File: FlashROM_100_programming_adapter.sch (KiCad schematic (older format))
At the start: 5 parts, among them J1 LH535618 DIP LEGS, U1 28C256

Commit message: Add FlashROM_100. /WE pin on FlexROM_100
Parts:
- removed JP1: ~CS~ breakout (REX TP1), 000_LOCAL:Pin_Header_Angled_1x02_Pitch2.54mm, symbol 000_LOCAL:Jumper_2_Bridged
- removed R1, R2: 47K, 000_LOCAL:R_0805, symbol 000_LOCAL:R_US
- J1: value LH535618 DIP LEGS -> LH535618 Socket; footprint 000_LOCAL:DIP28_0.6_pcb_sil_pins -> 000_LOCAL:DIP28_0.6
- U1: value 28C256 -> 29F010 pinout to programmer; footprint 000_LOCAL:SOIC28W -> 000_LOCAL:DIP32_0.3; symbol 000_LOCAL:28C256 -> 000_LOCAL:SST39SF010_PLCC
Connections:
- net ~CS_IN is gone; now on net D6: U1.20 (DQ6)
- net A0: now also U1.12 (A0); no longer U1.10 (A0)
- net A1: now also U1.11 (A1); no longer U1.9 (A1)
- net A10: now also U1.23 (A10); no longer U1.21 (A10)
- net A11: now also U1.25 (A11); no longer U1.23 (A11)
- net A12: now also U1.4 (A12); no longer U1.2 (A12)
- net A13: now also U1.28 (A13); no longer U1.26 (A13)
- net A14: now also U1.29 (A14); no longer U1.1 (A14)
- net A2: now also U1.10 (A2); no longer U1.8 (A2)
- net A3: now also U1.9 (A3); no longer U1.7 (A3)
- net A4: now also U1.8 (A4); no longer U1.6 (A4)
- net A5: now also U1.7 (A5); no longer U1.5 (A5)
- net A6: now also U1.6 (A6); no longer U1.4 (A6)
- net A7: now also U1.5 (A7); no longer U1.3 (A7)
- net A8: now also U1.27 (A8); no longer U1.25 (A8)
- net A9: now also U1.26 (A9); no longer U1.24 (A9)
- net D0: now also U1.13 (DQ0); no longer U1.11 (D0)
- net D1: now also U1.14 (DQ1); no longer U1.12 (D1)
- net D2: now also U1.15 (DQ2); no longer U1.13 (D2)
- net D3: now also U1.17 (DQ3); no longer U1.15 (D3)
- net D4: now also U1.18 (DQ4); no longer U1.16 (D4)
- net D5: now also U1.19 (DQ5); no longer U1.17 (D5)
- net D6: no longer U1.18 (D6)
- net D7: now also U1.21 (DQ7); no longer U1.19 (D7)
- net GND: now also U1.16 (VSS); no longer U1.14 (GND)
- net VCC: now also U1.32 (VDD); no longer U1.28 (VCC)
- net ~OE: now also U1.24 (~OE); no longer U1.22 (~OE)
- net ~WE: now also U1.31 (~WE); no longer U1.27 (~WE)
- net ~CS_OUT renamed ~CE
- net ~CE: now also U1.22 (~CE)
- no-connect marks 0 -> 4
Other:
- note added: "FlashROM_100 programming adapter.\n\nPlace this board into programmer.\nPlace FlashROM_100 into the DIP-28 socket.\n\nThis for the 29F010 FlashROM_100, not the 28C256 FlexROM_100."
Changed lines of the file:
@@
 encoding utf-8
 Sheet 1 1
-Title "28C256 SOIC to LH535618 DIP"
-Date ""
+Title "29F010 to LH535618 programming adapter"
+Date "2020-11-05"
 Rev ""
-Comp ""
-Comment1 "TRS-80 Model 100 system rom M12"
-Comment2 "With REX main ROM support"
+Comp "b.kenyon.w@gmail.com"
+Comment1 ""
+Comment2 ""
 Comment3 ""
 Comment4 ""
 $EndDescr
 $Comp
-L 000_LOCAL:28C256 U1
+L 000_LOCAL:SST39SF010_PLCC U1
 U 1 1 5E5B130A
-P 6670 3040
-F 0 "U1" H 6810 4160 50  0000 C CNN
-F 1 "28C256" H 6670 4350 50  0000 C CNN
-F 2 "000_LOCAL:SOIC28W" H 6670 3040 50  0001 C CNN
-F 3 "http://ww1.microchip.com/downloads/en/DeviceDoc/doc0006.pdf" H 6670 3040 50  0001 C CNN
-	1    6670 3040
+P 6700 3340
+F 0 "U1" H 6840 4460 50  0000 C CNN
+F 1 "29F010 pinout to programmer" H 6700 5060 50  0000 C CNN
+F 2 "000_LOCAL:DIP32_0.3" H 6700 3340 50  0001 C CNN
+F 3 "http://ww1.microchip.com/downloads/en/DeviceDoc/doc0006.pdf" H 6700 3340 50  0001 C CNN
+	1    6700 3340
 	1    0    0    -1
 $EndComp
@@
 P 4260 3040
 F 0 "J1" H 4440 4190 50  0000 C CNN
-F 1 "LH535618 DIP LEGS" H 4260 4420 50  0000 C CNN
-F 2 "000_LOCAL:DIP28_0.6_pcb_sil_pins" H 4260 3040 50  0001 C CNN
+F 1 "LH535618 Socket" H 4260 4420 50  0000 C CNN
+F 2 "000_LOCAL:DIP28_0.6" H 4260 3040 50  0001 C CNN
 F 3 "http://ww1.microchip.com/downloads/en/DeviceDoc/doc0014.pdf" H 4260 3040 50  0001 C CNN
 	1    4260 3040
@@
 	3400 3840 3500 3940
 Entry Wire Line
-	5830 1840 5930 1940
-Entry Wire Line
-	5830 3640 5930 3740
-Entry Wire Line
-	5830 4040 5930 4140
+	5830 1890 5930 1990
+Entry Wire Line
+	5830 4140 5930 4240
 Entry Wire Line
 	5830 2140 5930 2240
@@
 Entry Wire Line
 	5830 3440 5930 3540
-Text Label 5930 1940 0    50   ~ 0
+Text Label 5930 1990 0    50   ~ 0
 VCC
-Text Label 5930 3740 0    50   ~ 0
+Text Label 5930 4240 0    50   ~ 0
 ~WE
-Text Label 5930 4140 0    50   ~ 0
-GND
-Entry Wire Line
-	5830 3740 5930 3840
-Entry Wire Line
-	5830 3840 5930 3940
+Entry Wire Line
+	5830 4340 5930 4440
+Entry Wire Line
+	5830 4240 5930 4340
 Entry Wire Line
 	3400 1840 3500 1940
@@
 ~OE
 Text Label 3500 3940 0    50   ~ 0
-~CS_OUT
-Text Label 5930 3840 0    50   ~ 0
+~CE
+Text Label 5930 4440 0    50   ~ 0
 ~OE
-Text Label 5930 3940 0    50   ~ 0
-~CS_IN
+Text Label 5930 4340 0    50   ~ 0
+~CE
 Text Label 3500 2240 0    50   ~ 0
 A1
@@
 D7
 Entry Wire Line
-	7300 2140 7400 2040
-Entry Wire Line
-	7300 2240 7400 2140
-Entry Wire Line
-	7300 2340 7400 2240
-Entry Wire Line
-	7300 2440 7400 2340
-Entry Wire Line
-	7300 2540 7400 2440
-Entry Wire Line
-	7300 2640 7400 2540
-Entry Wire Line
-	7300 2740 7400 2640
-Entry Wire Line
-	7300 2840 7400 2740
-Text Label 7300 2140 2    50   ~ 0
+	7530 2140 7630 2040
+Entry Wire Line
+	7530 2240 7630 2140
+Entry Wire Line
+	7530 2340 7630 2240
+Entry Wire Line
+	7530 2440 7630 2340
+Entry Wire Line
+	7530 2540 7630 2440
+Entry Wire Line
+	7530 2640 7630 2540
+Entry Wire Line
+	7530 2740 7630 2640
+Entry Wire Line
+	7530 2840 7630 2740
+Text Label 7530 2140 2    50   ~ 0
 D0
-Text Label 7300 2240 2    50   ~ 0
+Text Label 7530 2240 2    50   ~ 0
 D1
-Text Label 7300 2340 2    50   ~ 0
+Text Label 7530 2340 2    50   ~ 0
 D2
-Text Label 7300 2440 2    50   ~ 0
+Text Label 7530 2440 2    50   ~ 0
 D3
-Text Label 7300 2540 2    50   ~ 0
+Text Label 7530 2540 2    50   ~ 0
 D4
-Text Label 7300 2640 2    50   ~ 0
+Text Label 7530 2640 2    50   ~ 0
 D5
-Text Label 7300 2740 2    50   ~ 0
+Text Label 7530 2740 2    50   ~ 0
 D6
-Text Label 7300 2840 2    50   ~ 0
+Text Label 7530 2840 2    50   ~ 0
 D7
-Entry Wire Line
-	3400 4570 3500 4670
-Entry Wire Line
-	3400 4670 3500 4770
-$Comp
-L 000_LOCAL:Jumper_2_Bridged JP1
-U 1 1 5E68B8A2
-P 4020 4670
-F 0 "JP1" H 4020 4750 50  0000 C CNN
-F 1 "~CS~ breakout (REX TP1)" H 4020 4830 50  0000 C CNN
-F 2 "000_LOCAL:Pin_Header_Angled_1x02_Pitch2.54mm" H 4020 4670 50  0001 C CNN
-F 3 "~" H 4020 4670 50  0001 C CNN
-	1    4020 4670
-	-1   0    0    -1
-$EndComp
-Entry Wire Line
-	3400 4770 3500 4870
-$Comp
-L 000_LOCAL:R_US R2
-U 1 1 5E68C7F8
-P 4080 4870
-F 0 "R2" V 4040 4550 50  0000 C CNN
-F 1 "47K" V 4040 4700 50  0000 C CNN
-F 2 "000_LOCAL:R_0805" H 4080 4870 50  0001 C CNN
-F 3 "~" H 4080 4870 50  0001 C CNN
-	1    4080 4870
-	0    1    1    0
-$EndComp
-Wire Wire Line
-	3500 4670 3820 4670
-Text Label 3500 4670 0    50   ~ 0
-~CS_OUT
-Wire Wire Line
-	3500 4870 3930 4870
-Text Label 3500 4770 0    50   ~ 0
-~CS_IN
-Text Label 3500 4870 0    50   ~ 0
-VCC
 Wire Bus Line
 	3400 5540 4980 5540
-Connection ~ 5830 5540
-Wire Bus Line
-	5830 5540 7400 5540
-Entry Wire Line
-	3400 5070 3500 5170
-Entry Wire Line
-	3400 5170 3500 5270
-$Comp
-L 000_LOCAL:R_US R1
-U 1 1 5E6B3AF8
-P 4080 5270
-F 0 "R1" V 4030 4900 50  0000 C CNN
-F 1 "47K" V 4030 5040 50  0000 C CNN
-F 2 "000_LOCAL:R_0805" H 4080 5270 50  0001 C CNN
-F 3 "~" H 4080 5270 50  0001 C CNN
-	1    4080 5270
-	0    1    1    0
-$EndComp
-Wire Wire Line
-	3500 5270 3930 5270
-Wire Wire Line
-	4230 5270 4230 5170
-Text Label 3500 5270 0    50   ~ 0
-VCC
-Text Label 3500 5170 0    50   ~ 0
-~WE
 Connection ~ 4980 5540
-Wire Bus Line
-	4980 5540 5830 5540
-Wire Bus Line
-	5830 5540 6590 5540
 Wire Wire Line
 	3500 1940 4260 1940
@@
 	4660 2840 4880 2840
 Wire Wire Line
-	5930 1940 6670 1940
-Wire Wire Line
-	5930 2140 6270 2140
-Wire Wire Line
-	5930 2240 6270 2240
-Wire Wire Line
-	5930 2340 6270 2340
-Wire Wire Line
-	5930 2440 6270 2440
-Wire Wire Line
-	5930 2540 6270 2540
-Wire Wire Line
-	5930 2640 6270 2640
-Wire Wire Line
-	5930 2740 6270 2740
-Wire Wire Line
-	5930 2840 6270 2840
-Wire Wire Line
-	5930 2940 6270 2940
-Wire Wire Line
-	5930 3040 6270 3040
-Wire Wire Line
-	5930 3140 6270 3140
-Wire Wire Line
-	5930 3240 6270 3240
-Wire Wire Line
-	5930 3340 6270 3340
-Wire Wire Line
-	5930 3440 6270 3440
-Wire Wire Line
-	5930 3540 6270 3540
-Wire Wire Line
-	5930 3740 6270 3740
-Wire Wire Line
-	5930 3840 6270 3840
-Wire Wire Line
-	5930 3940 6270 3940
-Wire Wire Line
-	5930 4140 6670 4140
-Wire Wire Line
-	7070 2140 7300 2140
-Wire Wire Line
-	7070 2240 7300 2240
-Wire Wire Line
-	7070 2340 7300 2340
-Wire Wire Line
-	7070 2440 7300 2440
-Wire Wire Line
-	7070 2540 7300 2540
-Wire Wire Line
-	7070 2640 7300 2640
-Wire Wire Line
-	7070 2740 7300 2740
-Wire Wire Line
-	7070 2840 7300 2840
-Wire Wire Line
-	4360 4670 4360 4770
-Wire Wire Line
-	4230 4870 4360 4870
-Wire Wire Line
-	3500 4770 4360 4770
-Connection ~ 4360 4770
-Wire Wire Line
-	4360 4770 4360 4870
-Wire Wire Line
-	4360 4670 4220 4670
-Wire Wire Line
-	3500 5170 4230 5170
+	7300 2140 7530 2140
+Wire Wire Line
+	7300 2240 7530 2240
+Wire Wire Line
+	7300 2340 7530 2340
+Wire Wire Line
+	7300 2440 7530 2440
+Wire Wire Line
+	7300 2540 7530 2540
+Wire Wire Line
+	7300 2640 7530 2640
+Wire Wire Line
+	7300 2740 7530 2740
+Wire Wire Line
+	7300 2840 7530 2840
 Entry Wire Line
 	3400 3640 3500 3740
 Wire Wire Line
-	3500 3740 3860 3740
-Wire Bus Line
-	4980 2040 4980 5540
-Wire Bus Line
-	7400 2040 7400 5540
-Wire Bus Line
-	5830 1840 5830 5540
-Wire Bus Line
-	3400 1840 3400 5540
+	3860 3740 3500 3740
 Text Label 3500 3740 0    50   ~ 0
 ~WE
+NoConn ~ 6100 3740
+NoConn ~ 6100 3640
+Entry Wire Line
+	5830 4490 5930 4590
+Text Label 5930 4590 0    50   ~ 0
+GND
+Wire Wire Line
+	5930 1990 6700 1990
+Wire Wire Line
+	5930 2140 6100 2140
+Wire Wire Line
+	5930 2240 6100 2240
+Wire Wire Line
+	5930 2340 6100 2340
+Wire Wire Line
+	5930 2440 6100 2440
+Wire Wire Line
+	5930 2540 6100 2540
+Wire Wire Line
+	5930 2640 6100 2640
+Wire Wire Line
+	5930 2740 6100 2740
+Wire Wire Line
+	5930 2840 6100 2840
+Wire Wire Line
+	5930 2940 6100 2940
+Wire Wire Line
+	5930 3040 6100 3040
+Wire Wire Line
+	5930 3140 6100 3140
+Wire Wire Line
+	5930 3240 6100 3240
+Wire Wire Line
+	5930 3340 6100 3340
+Wire Wire Line
+	5930 3440 6100 3440
+Wire Wire Line
+	5930 3540 6100 3540
+Wire Wire Line
+	5930 4240 6100 4240
+Wire Wire Line
+	5930 4340 6100 4340
+Wire Wire Line
+	5930 4440 6100 4440
+Wire Wire Line
+	5930 4590 6700 4590
+NoConn ~ 7300 4340
+NoConn ~ 7300 4440
+Wire Bus Line
+	4980 5540 7630 5540
+Wire Bus Line
+	4980 2040 4980 5540
+Wire Bus Line
+	7630 2040 7630 5540
+Wire Bus Line
+	3400 1840 3400 5540
+Wire Bus Line
+	5830 1890 5830 5540
+Text Notes 4440 6170 0    50   ~ 0
+FlashROM_100 programming adapter.\n\nPlace this board into programmer.\nPlace FlashROM_100 into the DIP-28 socket.\n\nThis for the 29F010 FlashROM_100, not the 28C256 FlexROM_100.
 $EndSCHEMATC

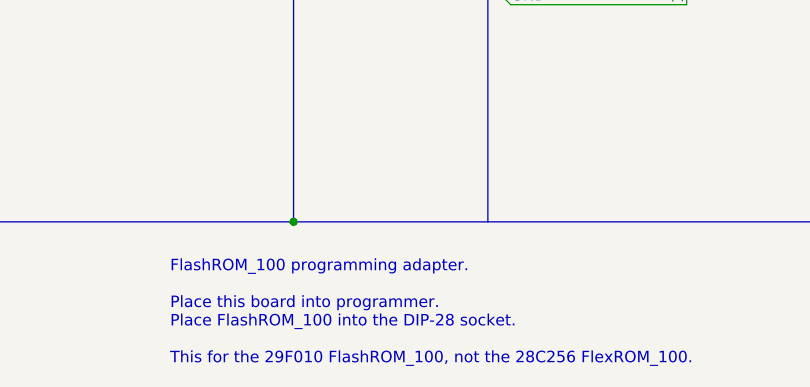
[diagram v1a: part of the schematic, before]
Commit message: FlexROM_100 & FlashROM_100 fix ALE/WE
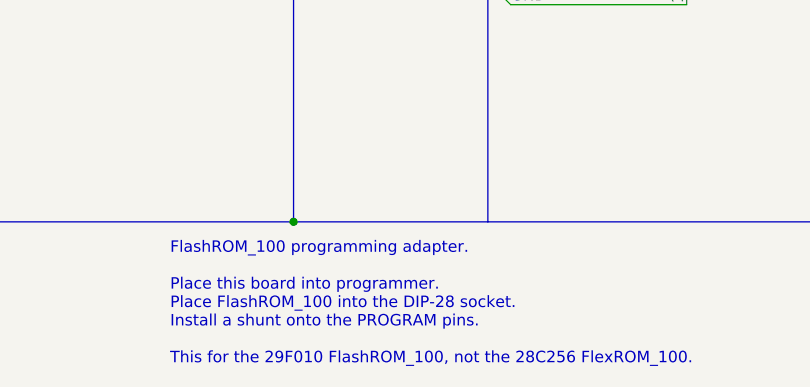
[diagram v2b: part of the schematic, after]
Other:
- note added: "FlashROM_100 programming adapter.\n\nPlace this board into programmer.\nPlace FlashROM_100 into the DIP-28 socket.\nInstall a shunt onto the PROGRAM pins.\n\nThis for the 29F010 FlashROM_100, not the 28C256 FlexROM_100."
- note removed: "FlashROM_100 programming adapter.\n\nPlace this board into programmer.\nPlace FlashROM_100 into the DIP-28 socket.\n\nThis for the 29F010 FlashROM_100, not the 28C256 FlexROM_100."
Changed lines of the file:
@@
 Sheet 1 1
 Title "29F010 to LH535618 programming adapter"
-Date "2020-11-05"
+Date "2020-11-23"
 Rev ""
 Comp "b.kenyon.w@gmail.com"
@@
 Wire Bus Line
 	4980 5540 7630 5540
+Text Notes 4440 6170 0    50   ~ 0
+FlashROM_100 programming adapter.\n\nPlace this board into programmer.\nPlace FlashROM_100 into the DIP-28 socket.\nInstall a shunt onto the PROGRAM pins.\n\nThis for the 29F010 FlashROM_100, not the 28C256 FlexROM_100.
 Wire Bus Line
 	4980 2040 4980 5540
@@
 Wire Bus Line
 	5830 1890 5830 5540
-Text Notes 4440 6170 0    50   ~ 0
-FlashROM_100 programming adapter.\n\nPlace this board into programmer.\nPlace FlashROM_100 into the DIP-28 socket.\n\nThis for the 29F010 FlashROM_100, not the 28C256 FlexROM_100.
 $EndSCHEMATC

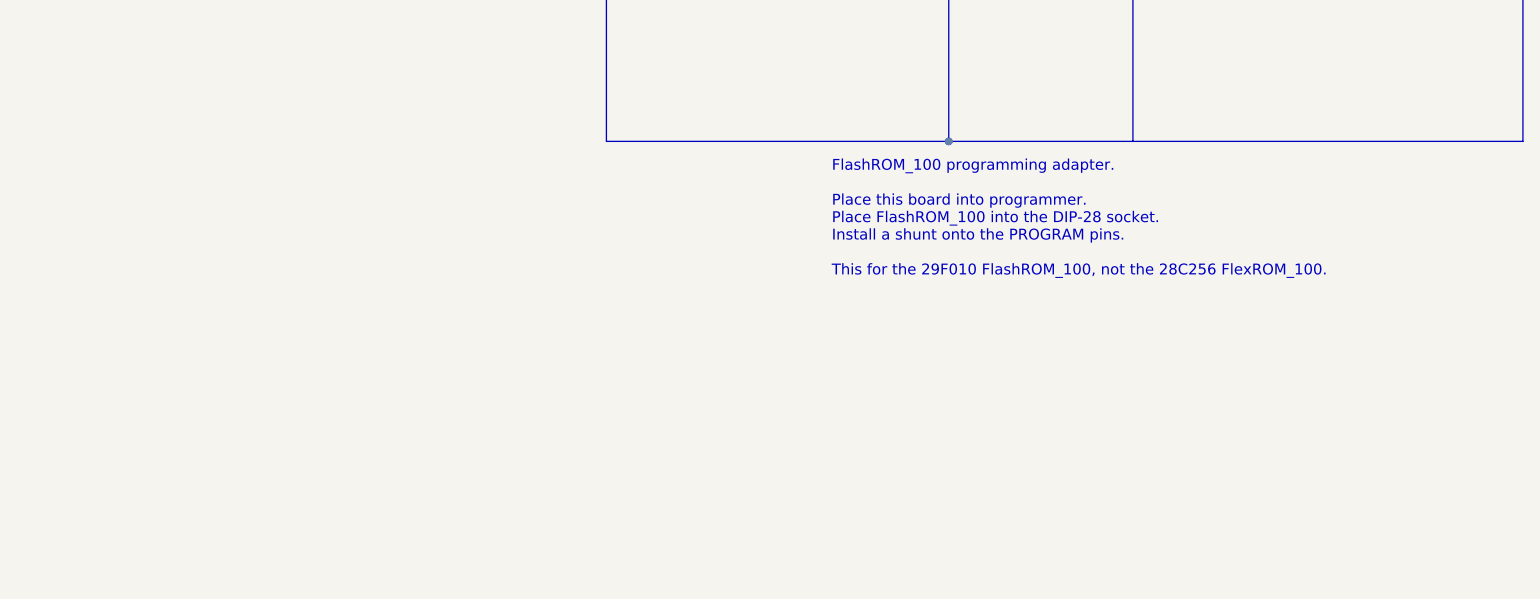
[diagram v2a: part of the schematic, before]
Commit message: simpler programming adapters, update pics and BOMs
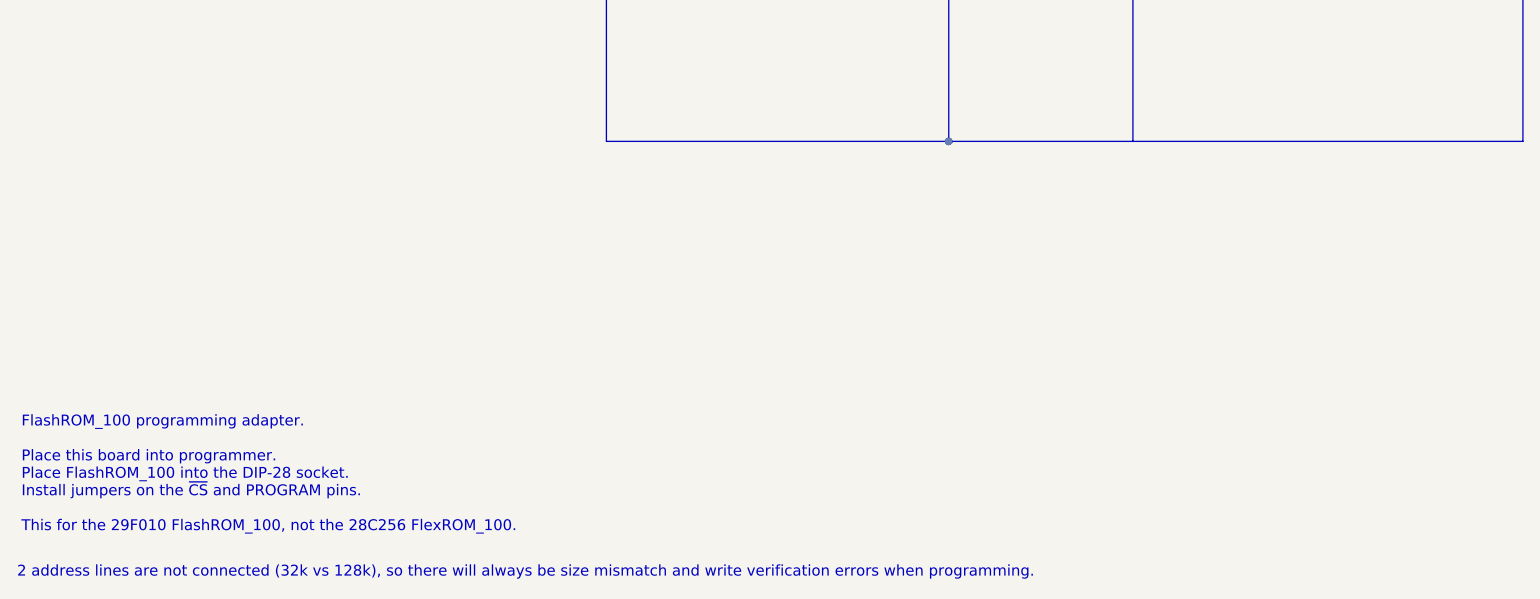
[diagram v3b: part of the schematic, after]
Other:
- note added: "2 address lines are not connected (32k vs 128k), so there will always be size mismatch and write verification errors when programming."
- note added: "FlashROM_100 programming adapter.\n\nPlace this board into programmer.\nPlace FlashROM_100 into the DIP-28 socket.\nInstall jumpers on the ~CS~ and PROGRAM pins.\n\nThis for the 29F010 FlashROM_100, not the 28C256 FlexROM_100."
- note removed: "FlashROM_100 programming adapter.\n\nPlace this board into programmer.\nPlace FlashROM_100 into the DIP-28 socket.\nInstall a shunt onto the PROGRAM pins.\n\nThis for the 29F010 FlashROM_100, not the 28C256 FlexROM_100."
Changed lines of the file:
@@
 Wire Bus Line
 	4980 5540 7630 5540
-Text Notes 4440 6170 0    50   ~ 0
-FlashROM_100 programming adapter.\n\nPlace this board into programmer.\nPlace FlashROM_100 into the DIP-28 socket.\nInstall a shunt onto the PROGRAM pins.\n\nThis for the 29F010 FlashROM_100, not the 28C256 FlexROM_100.
 Wire Bus Line
 	4980 2040 4980 5540
@@
 Wire Bus Line
 	5830 1890 5830 5540
+Text Notes 700  7350 0    50   ~ 0
+FlashROM_100 programming adapter.\n\nPlace this board into programmer.\nPlace FlashROM_100 into the DIP-28 socket.\nInstall jumpers on the ~CS~ and PROGRAM pins.\n\nThis for the 29F010 FlashROM_100, not the 28C256 FlexROM_100.
+Text Notes 680  7560 0    50   ~ 0
+2 address lines are not connected (32k vs 128k), so there will always be size mismatch and write verification errors when programming.
 $EndSCHEMATC
